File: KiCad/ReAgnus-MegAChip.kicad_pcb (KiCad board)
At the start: 2 copper layers, 78 x 49 mm, 38 parts, among them J2 Conn_02x05_Odd_Even, J3 Conn_02x01, J4 Conn_01x01, J5 Conn_01x01, J6 Conn_01x01, J7 Conn_01x01, U1 PLCC-84-Plug, U10 AS4C4M16SA, U2 LM1117-3.3, U3 SN74CBTD16210, U4 SN74CBTD16210, U5 SN74CBTD16210, U6 SN74CBTD16210, U7 GW1N-UV9LQ144, U8 74LVC1G07, U9 Agnus_TH_plug_pins

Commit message: more routing and placing components
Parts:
- added C19: 0.01uF, Capacitor_SMD:C_0805_2012Metric_Pad1.15x1.40mm_HandSolder, F.Cu at (157.8, 118.3)
- moved C9 54.5 mm to (173.2, 132.3), turned to 270 degrees
- moved C10 43.6 mm to (165.1, 124.5), turned to 135 degrees
- moved C11 37.7 mm to (157.8, 116.4), turned to 180 degrees
- moved C12 23.9 mm to (163.6, 105.4), turned to 135 degrees
- moved C18 1.75 mm to (175.1, 132.3)
- moved C1 0.83 mm to (161.8, 94.6)
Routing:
- net 3V3: track 248.0 -> 324.3 mm, vias 10 -> 15
- net GND: track 25.9 -> 39.2 mm, vias 27 -> 36
- net INTR_3V3: track 29.3 -> 30.9 mm
- net A13_3V3: track 27.9 -> 28.8 mm
- net DRD15_3V3: track 19.0 -> 19.8 mm
- net A12_3V3: track 29.7 -> 30.4 mm
- net DRD12_3V3: track 24.3 -> 25.0 mm
- net A5_3V3: track 26.5 -> 27.1 mm

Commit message: more routing
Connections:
- net Net-(U10-Pad29) renamed A4_SDRAM
- net Net-(U10-Pad30) renamed A5_SDRAM
- net Net-(U10-Pad31) renamed A6_SDRAM
- net Net-(U10-Pad32) renamed A7_SDRAM
- net Net-(U10-Pad33) renamed A8_SDRAM
- net Net-(U10-Pad34) renamed A9_SDRAM
- net Net-(U10-Pad35) renamed A11_SDRAM
- U10 pad 10: DRD14_3V3 -> DRD5_3V3
- U10 pad 11: DRD15_3V3 -> DRD6_3V3
- U10 pad 13: DRD8_3V3 -> DRD7_3V3
- U10 pad 2: DRD9_3V3 -> DRD0_3V3
- U10 pad 22: Net-(U10-Pad22) -> A10_SDRAM
- U10 pad 23: Net-(U10-Pad23) -> A0_SDRAM
- U10 pad 24: Net-(U10-Pad24) -> A1_SDRAM
- U10 pad 25: Net-(U10-Pad25) -> A2_SDRAM
- U10 pad 26: Net-(U10-Pad26) -> A3_SDRAM
- U10 pad 4: DRD10_3V3 -> DRD1_3V3
- U10 pad 42: DRD7_3V3 -> DRD8_3V3
- U10 pad 44: DRD6_3V3 -> DRD9_3V3
- U10 pad 45: DRD5_3V3 -> DRD10_3V3
- U10 pad 47: DRD4_3V3 -> DRD11_3V3
- U10 pad 48: DRD3_3V3 -> DRD12_3V3
- U10 pad 5: DRD11_3V3 -> DRD2_3V3
- U10 pad 50: DRD2_3V3 -> DRD13_3V3
- U10 pad 51: DRD1_3V3 -> DRD14_3V3
- U10 pad 53: DRD0_3V3 -> DRD15_3V3
- U10 pad 7: DRD12_3V3 -> DRD3_3V3
- U10 pad 8: DRD13_3V3 -> DRD4_3V3
- U7 pad 137: Net-(U7-Pad137) -> A10_SDRAM
- U7 pad 138: Net-(U7-Pad138) -> A0_SDRAM
- U7 pad 139: Net-(U7-Pad139) -> A1_SDRAM
- U7 pad 140: Net-(U7-Pad140) -> A2_SDRAM
- U7 pad 141: Net-(U7-Pad141) -> A3_SDRAM
- U7 pad 142: Net-(U7-Pad142) -> JP1
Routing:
- net 3V3: track 324.3 -> 348.5 mm, vias 15 -> 17
- net DRD8_3V3: track 16.0 -> 34.0 mm, vias 0 -> 1
- net TCK: track 7.36 -> 24.5 mm, vias 0 -> 1
- net DRD7_3V3: track 17.1 -> 33.7 mm, vias 0 -> 1
- net DRD6_3V3: track 18.1 -> 32.3 mm, vias 0 -> 1
- net DRD9_3V3: track 19.5 -> 32.7 mm, vias 0 -> 1
- net DRD5_3V3: track 19.2 -> 31.6 mm, vias 0 -> 1
- net A10_SDRAM: track 0.00 -> 11.6 mm, vias 0 -> 1
- net A0_SDRAM: track 0.00 -> 11.1 mm, vias 0 -> 1
- net JP1: track 0.00 -> 11.0 mm, vias 0 -> 1
- net A1_SDRAM: track 0.00 -> 10.5 mm, vias 0 -> 1
- net A2_SDRAM: track 0.00 -> 9.97 mm, vias 0 -> 1
- net DRD4_3V3: track 20.2 -> 30.1 mm, vias 0 -> 1
- net DRD13_3V3: track 20.2 -> 29.7 mm, vias 0 -> 1
- net A3_SDRAM: track 0.00 -> 9.44 mm, vias 0 -> 1
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
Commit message: more routing
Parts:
- added J1: Conn_02x02_Odd_Even, Connector_PinHeader_2.00mm:PinHeader_2x02_P2.00mm_Vertical, F.Cu at (178.9, 133.1)
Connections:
- U10 pad 15: Net-(U10-Pad15) -> DQML_SDRAM
- U10 pad 16: Net-(U10-Pad16) -> WE_SDRAM
- U10 pad 17: Net-(U10-Pad17) -> CAS_SDRAM
- U10 pad 18: Net-(U10-Pad18) -> RAS_SDRAM
- U10 pad 19: Net-(U10-Pad19) -> CS_SDRAM
- U10 pad 20: Net-(U10-Pad20) -> BA0_SDRAM
- U10 pad 21: Net-(U10-Pad21) -> BA1_SDRAM
- U10 pad 37: Net-(U10-Pad37) -> CKE_SDRAM
- U10 pad 38: Net-(U10-Pad38) -> CLK_SDRAM
- U10 pad 39: Net-(U10-Pad39) -> DQMH_SDRAM
- U7 pad 119: Net-(U7-Pad119) -> DQMH_SDRAM
- U7 pad 120: Net-(U7-Pad120) -> DQML_SDRAM
- U7 pad 121: Net-(U7-Pad121) -> WE_SDRAM
- U7 pad 122: Net-(U7-Pad122) -> CKE_SDRAM
- U7 pad 123: GCLKT_1 -> CLK_SDRAM
- U7 pad 124: Net-(U7-Pad124) -> CAS_SDRAM
- U7 pad 125: Net-(U7-Pad125) -> RAS_SDRAM
- U7 pad 126: Net-(U7-Pad126) -> A11_SDRAM
- U7 pad 128: Net-(U7-Pad128) -> A9_SDRAM
- U7 pad 129: Net-(U7-Pad129) -> A8_SDRAM
- U7 pad 130: Net-(U7-Pad130) -> A7_SDRAM
- U7 pad 131: Net-(U7-Pad131) -> A6_SDRAM
- U7 pad 132: Net-(U7-Pad132) -> A5_SDRAM
- U7 pad 133: Net-(U7-Pad133) -> A4_SDRAM
- U7 pad 134: Net-(U7-Pad134) -> CS_SDRAM
- U7 pad 135: Net-(U7-Pad135) -> BA0_SDRAM
- U7 pad 136: Net-(U7-Pad136) -> BA1_SDRAM
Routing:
- net DQML_SDRAM: track 0.00 -> 19.7 mm, vias 0 -> 1
- net WE_SDRAM: track 0.00 -> 19.1 mm, vias 0 -> 1
- net CAS_SDRAM: track 0.00 -> 16.6 mm, vias 0 -> 1
- net RAS_SDRAM: track 0.00 -> 16.1 mm, vias 0 -> 1
- net CS_SDRAM: track 0.00 -> 14.3 mm, vias 0 -> 1
- net BA0_SDRAM: track 0.00 -> 13.7 mm, vias 0 -> 1
- net BA1_SDRAM: track 0.00 -> 13.2 mm, vias 0 -> 1
- net CLK_SDRAM: track 0.00 -> 11.0 mm, vias 0 -> 1
- net DQMH_SDRAM: track 0.00 -> 6.56 mm, vias 0 -> 1
- net A8_SDRAM: track 0.00 -> 6.04 mm, vias 0 -> 1
- net A11_SDRAM: track 0.00 -> 5.65 mm, vias 0 -> 1
- net A9_SDRAM: track 0.00 -> 5.23 mm, vias 0 -> 1
- net CKE_SDRAM: track 0.00 -> 4.71 mm, vias 0 -> 1
- net A5_SDRAM: track 0.00 -> 3.83 mm, vias 0 -> 1
- net A7_SDRAM: track 0.00 -> 3.83 mm, vias 0 -> 1
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
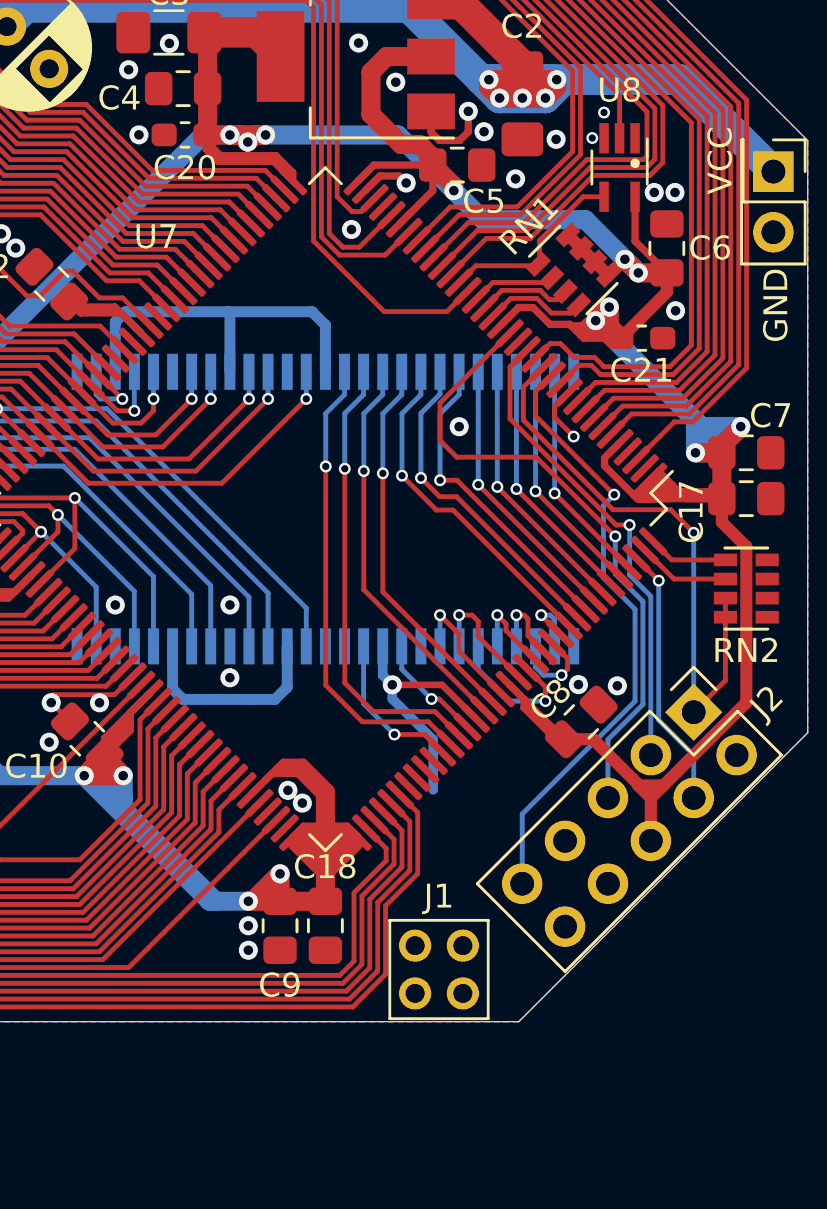
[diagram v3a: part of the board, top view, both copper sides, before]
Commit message: added Oscillator X1 for SDRAM and GCLKT_1 pin on FPGA
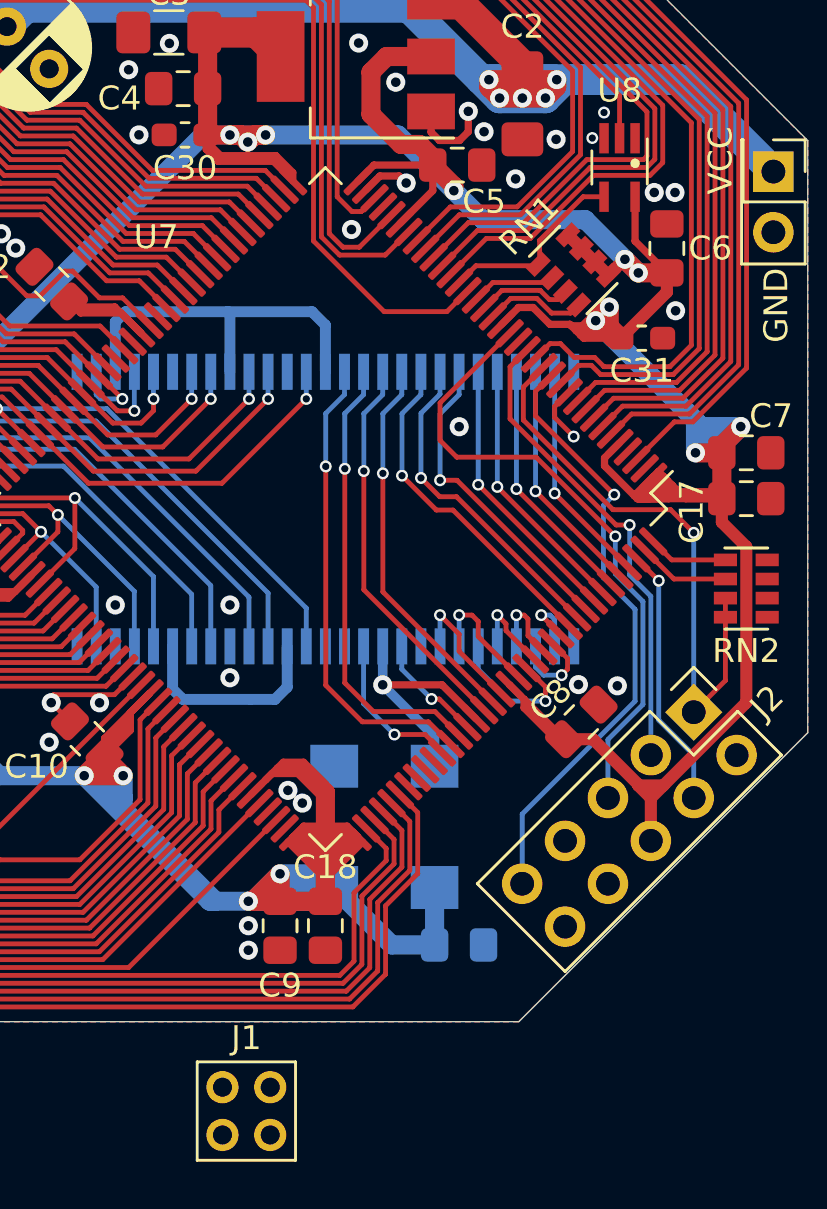
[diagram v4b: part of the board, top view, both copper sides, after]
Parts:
- added C20: 0.01uF, Capacitor_SMD:C_0805_2012Metric_Pad1.15x1.40mm_HandSolder, B.Cu at (180.7, 133.1)
- added X1: SG-8002CA, Oscillator:Oscillator_SMD_SeikoEpson_SG8002CA-4Pin_7.0x5.0mm, B.Cu at (177.6, 128.1)
- moved J1 10.0 mm to (170.8, 139.0)
- renumbered C20 to C30, C21 to C31
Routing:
- net 3V3: track 348.5 -> 366.3 mm
- net CLK_SDRAM: track 11.0 -> 10.4 mm

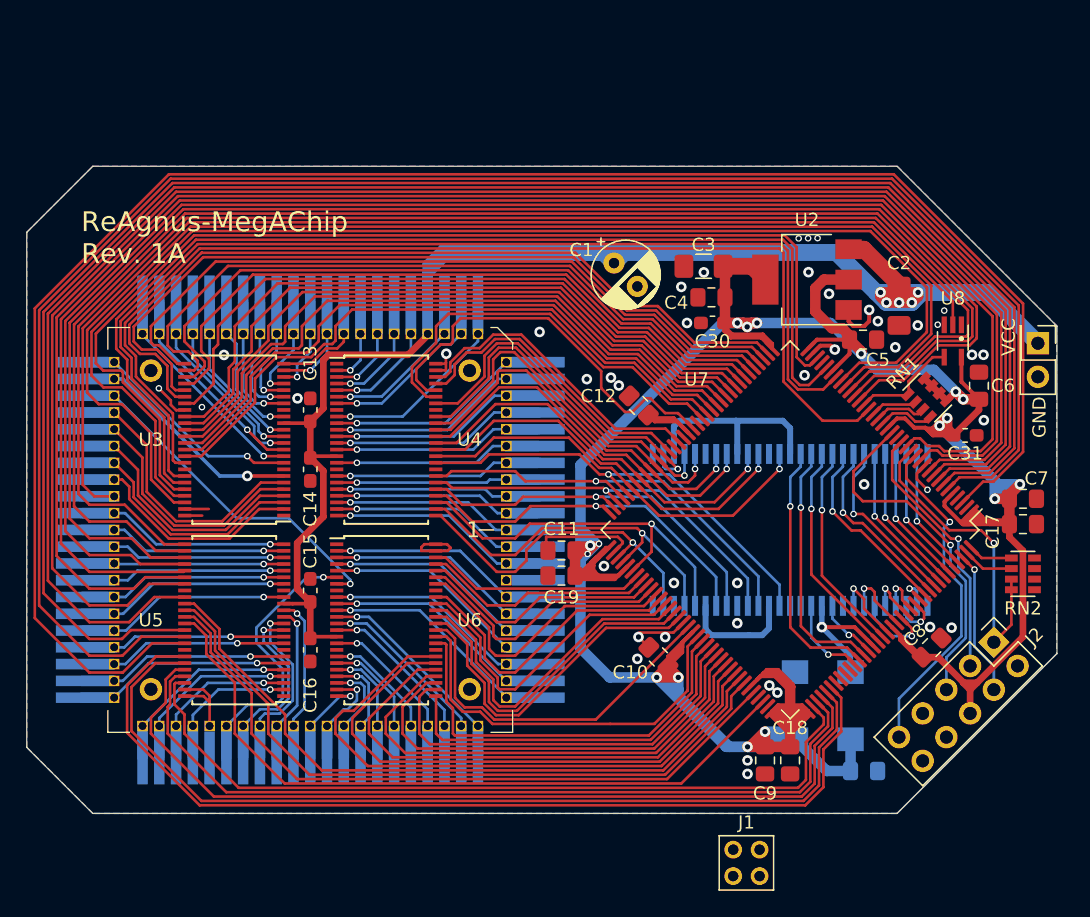
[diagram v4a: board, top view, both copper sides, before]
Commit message: added 74LVC245A IC for A20-A23 and more routing done
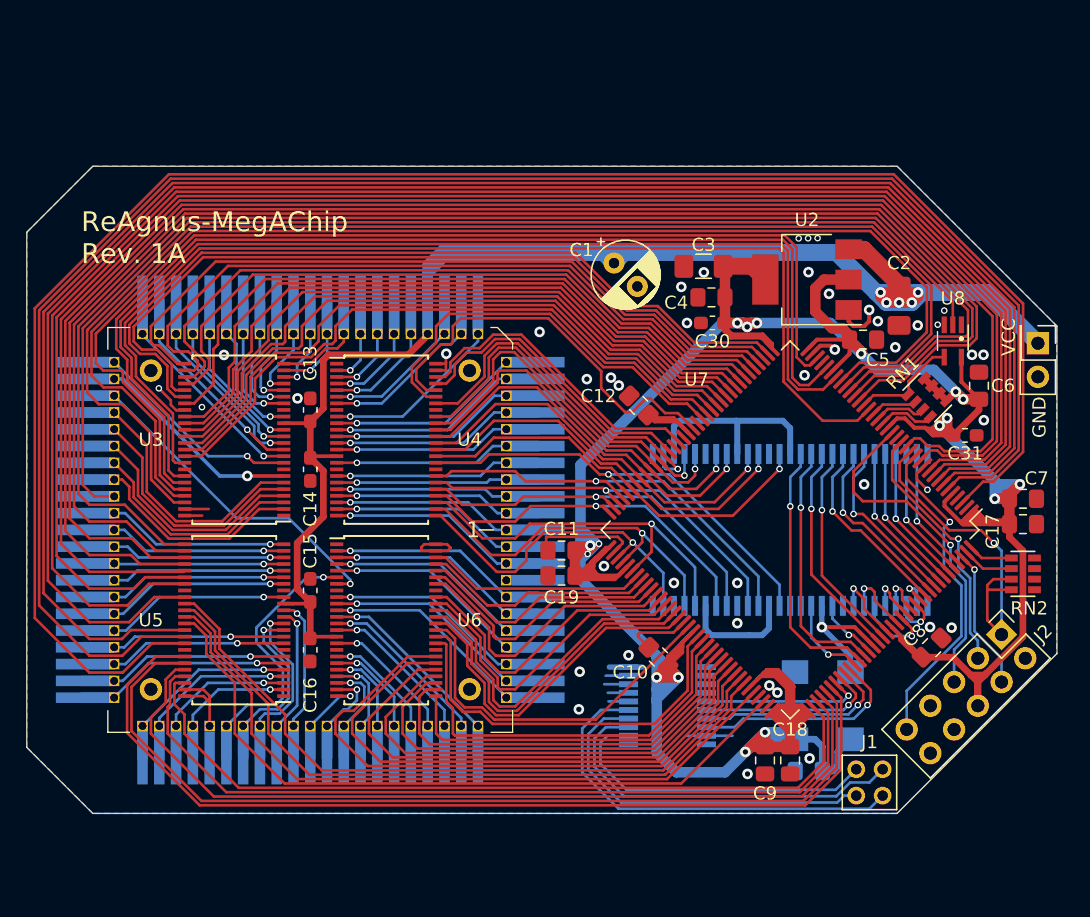
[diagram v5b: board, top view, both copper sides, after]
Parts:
- added U11: 74LVC245A, Package_SO:TSSOP-20_4.4x6.5mm_P0.65mm, B.Cu at (165.8, 128.1)
- moved J1 11.1 mm to (180.1, 133.0)
- moved C20 4.19 mm to (176.5, 133.1), turned to 180 degrees
- moved J2 0.82 mm to (191.1, 122.8)
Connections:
- J1 pad 2: A22 -> A21
- J1 pad 3: A21 -> A22
- U7 pad 115: Net-(U7-Pad115) -> A23_3V3
- U7 pad 116: Net-(U7-Pad116) -> A22_3V3
- U7 pad 117: Net-(U7-Pad117) -> A21_3V3
- U7 pad 118: Net-(U7-Pad118) -> A20_3V3
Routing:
- net A23: track 0.00 -> 31.7 mm
- net A21: track 0.00 -> 28.7 mm
- net A22: track 0.00 -> 27.8 mm
- net A20: track 0.00 -> 24.8 mm
- net A20_3V3: track 0.00 -> 16.4 mm, vias 0 -> 1
- net A21_3V3: track 0.00 -> 15.0 mm, vias 0 -> 1
- net A22_3V3: track 0.00 -> 13.6 mm, vias 0 -> 1
- net GND: track 39.2 -> 51.9 mm
- net A23_3V3: track 0.00 -> 12.3 mm, vias 0 -> 1
- net TCK: track 24.5 -> 26.9 mm
- net 3V3: track 366.3 -> 367.8 mm
- net TMS: track 25.6 -> 24.8 mm
- net TDO: track 26.7 -> 25.9 mm

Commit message: more routing and placing components
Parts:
- added U12: 74LVC1GX04, Package_SO:TSOP-6_1.65x3.05mm_P0.95mm, B.Cu at (192.5, 111.4)
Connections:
- U7 pad 56: GCLKT_5 -> JP2
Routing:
- net JP2: track 0.00 -> 41.5 mm, vias 0 -> 1
- net (no net): track 0.00 -> 19.8 mm
- net GCLKT_7: track 2.42 -> 9.40 mm
- net 3V3: track 367.8 -> 361.1 mm
- net TCK: track 26.9 -> 26.1 mm

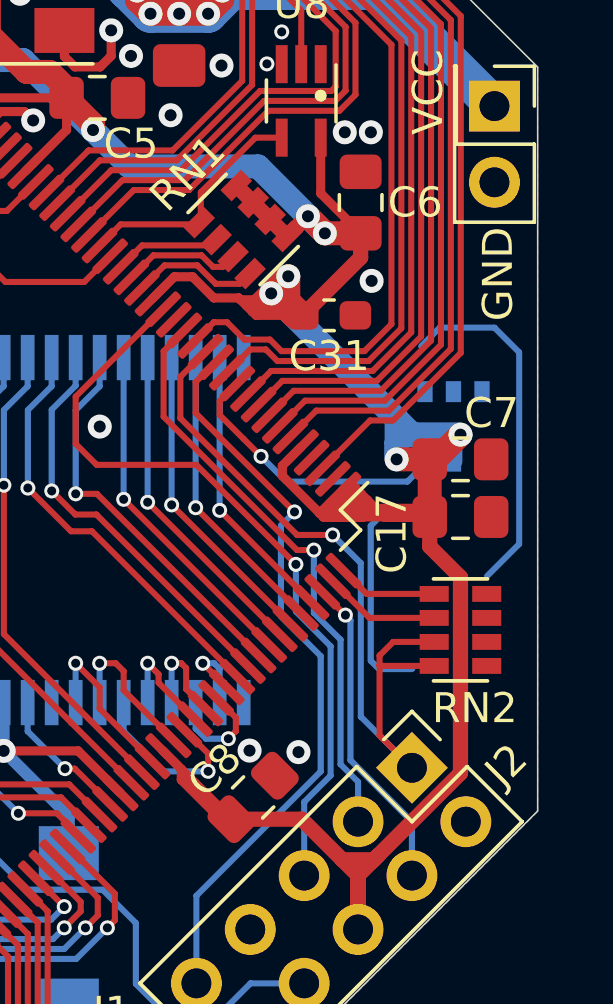
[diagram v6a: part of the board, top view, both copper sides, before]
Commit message: added optional Oscillator circuit with 28M crystal 3.2mm x 2.5mm x 0.8mm
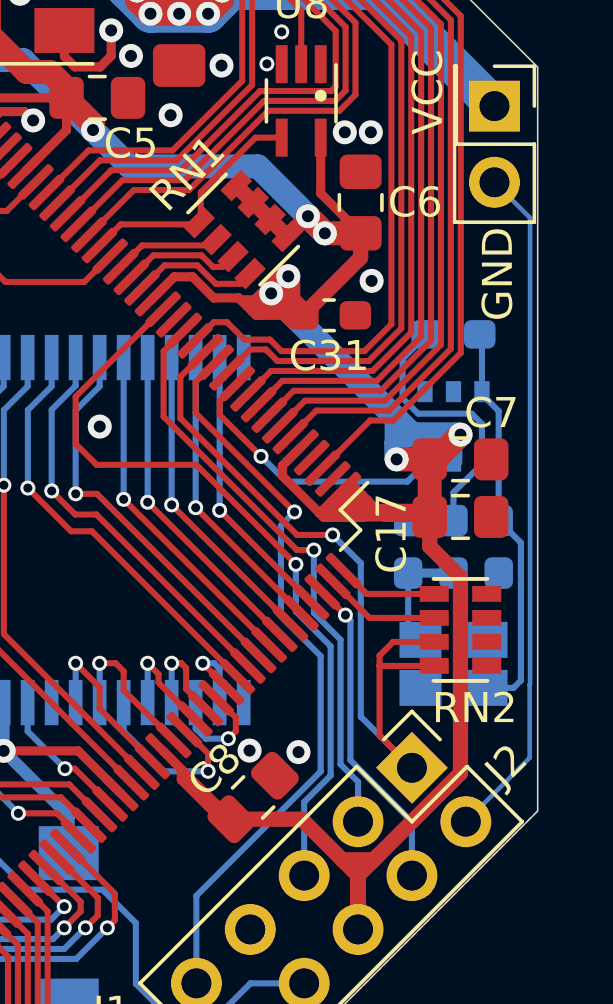
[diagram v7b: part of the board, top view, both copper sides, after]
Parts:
- added C40: 32pF, Capacitor_SMD:C_0603_1608Metric_Pad1.05x0.95mm_HandSolder, B.Cu at (194.0, 115.4)
- added C41: 32pF, Capacitor_SMD:C_0603_1608Metric_Pad1.05x0.95mm_HandSolder, B.Cu at (191.0, 115.4)
- added R1: 1kΩ, Resistor_SMD:R_0603_1608Metric_Pad1.05x0.95mm_HandSolder, B.Cu at (192.5, 115.4)
- added R2: 2.2MΩ, Resistor_SMD:R_0603_1608Metric_Pad1.05x0.95mm_HandSolder, B.Cu at (192.5, 108.3)
- added Y1: CL=16pF, Crystal:Crystal_SMD_SeikoEpson_FA238-4Pin_3.2x2.5mm, B.Cu at (192.5, 119.3)
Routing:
- net GND: track 51.9 -> 74.5 mm
- net (no net): track 19.8 -> 0.00 mm
- net Net-(C40-Pad1): track 0.00 -> 13.5 mm
- net Net-(R1-Pad1): track 0.00 -> 9.08 mm
- net Net-(C41-Pad1): track 0.00 -> 3.90 mm

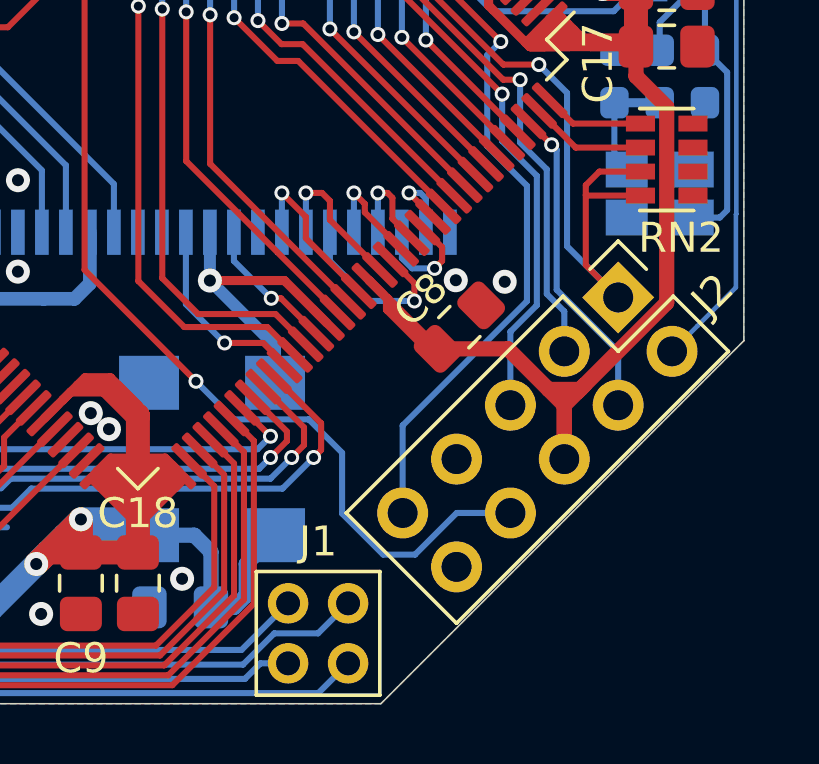
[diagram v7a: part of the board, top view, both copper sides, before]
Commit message: silkscreen fixes
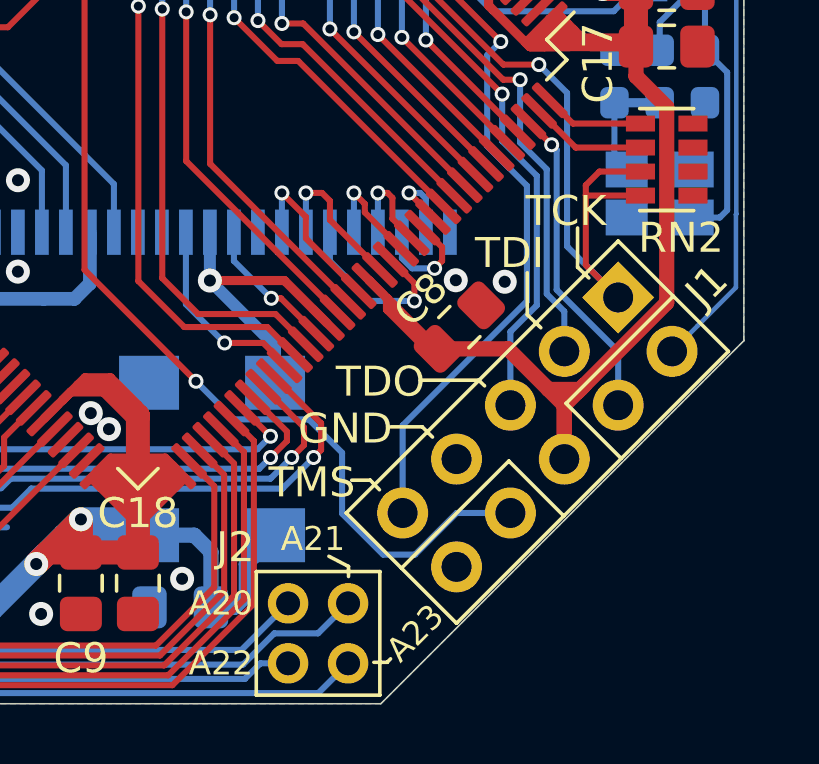
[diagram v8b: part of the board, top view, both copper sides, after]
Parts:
- removed the J2 at (191.1, 122.8)
- added J1: Conn_02x05_Odd_Even, Connector_PinHeader_2.54mm:PinHeader_2x05_P2.54mm_Vertical, F.Cu at (191.1, 122.8)
- renumbered J1 to J2
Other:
- board text added: "1kΩ"
- board text added: "2.2MΩ"
- board text added: "A20"
- board text added: "A21"
- board text added: "A22"
- board text added: "A23"
- board text added: "TCK"
- board text added: "TDI"
- board text added: "TDO"
- board text added: "TMS"
